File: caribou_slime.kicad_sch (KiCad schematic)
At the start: 38 parts, among them J1 BATT JST, Q1 AO3145, U1 ESP32-C3_SUPERMINI, U2 BMI270, U3 FS312F-G, U4 FS8205A, U5 TP4056, U6 ME6211C33M5G

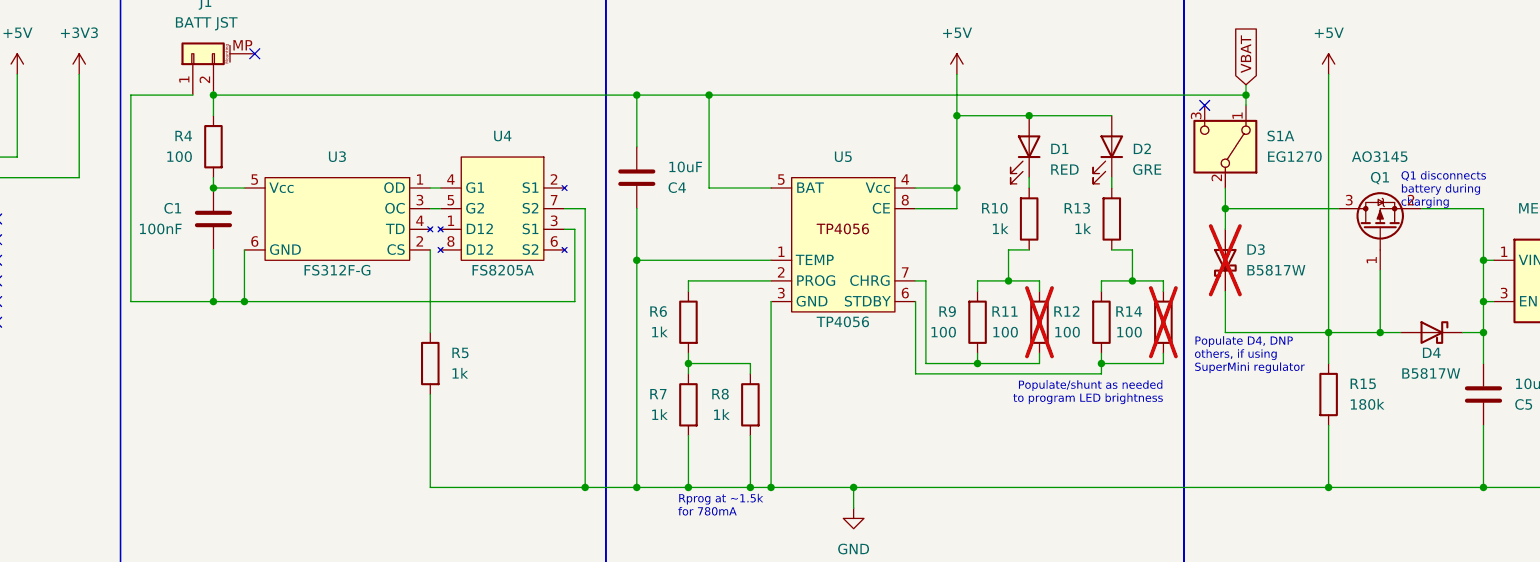
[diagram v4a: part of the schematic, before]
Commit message: fix(schematic): Make minor corrections to regulator circuit
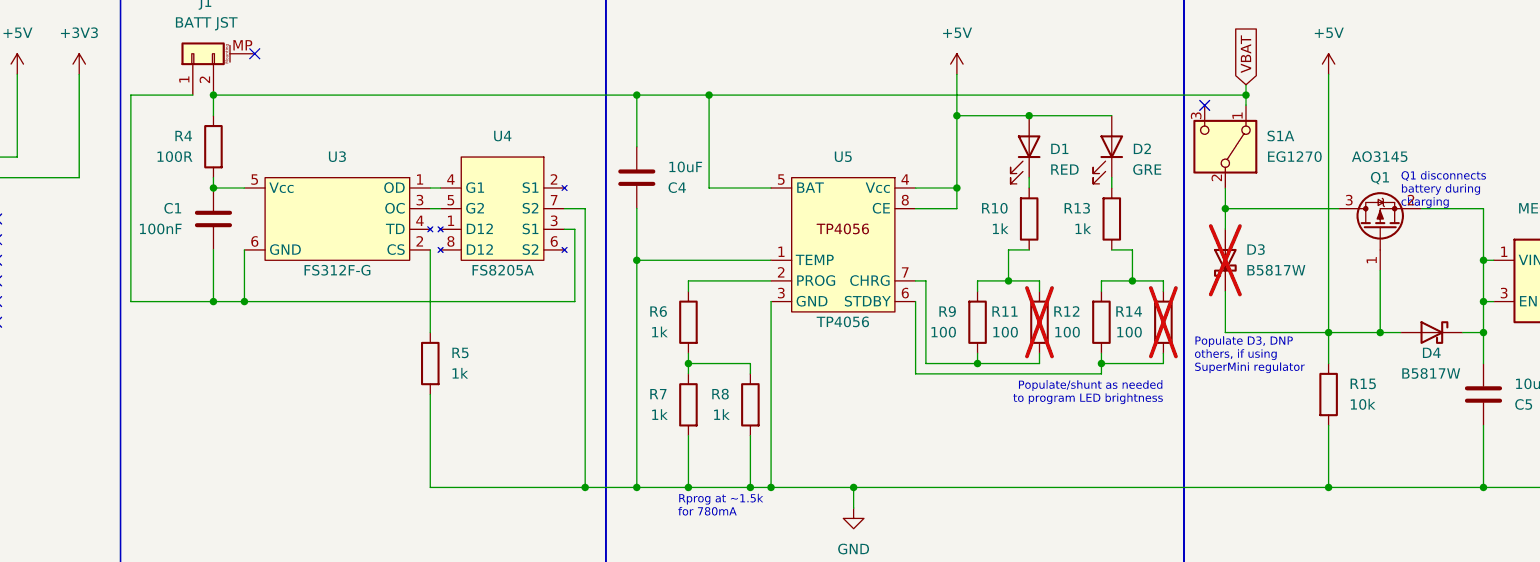
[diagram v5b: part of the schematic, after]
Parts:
- R15: value 180k -> 10k
- R4: value 100 -> 100R
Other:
- note added: "Populate D3, DNP others, if using SuperMini regulator"
- note removed: "Populate D4, DNP others, if using SuperMini regulator"
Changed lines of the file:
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@@
     (effects (font (size 1.27 1.27)) (justify left bottom))
   )
-  (text "Populate D4, DNP \nothers, if using\nSuperMini regulator"
+  (text "Populate D3, DNP \nothers, if using\nSuperMini regulator"
     (at 217.17 73.66 0)
     (effects (font (size 1 1)) (justify left bottom))
@@
       (effects (font (size 1.27 1.27)) (justify left))
     )
-    (property "Value" "100" (at 93.98 46.99 0)
+    (property "Value" "100R" (at 93.98 46.99 0)
       (effects (font (size 1.27 1.27)) (justify left))
     )
@@
       (effects (font (size 1.27 1.27)) (justify left))
     )
-    (property "Value" "180k" (at 236.22 77.47 0)
-      (effects (font (size 1.27 1.27)) (justify left))
-    )
+    (property "Value" "10k" (at 236.22 77.47 0)
+      (effects (font (size 1.27 1.27)) (justify left))
+    )

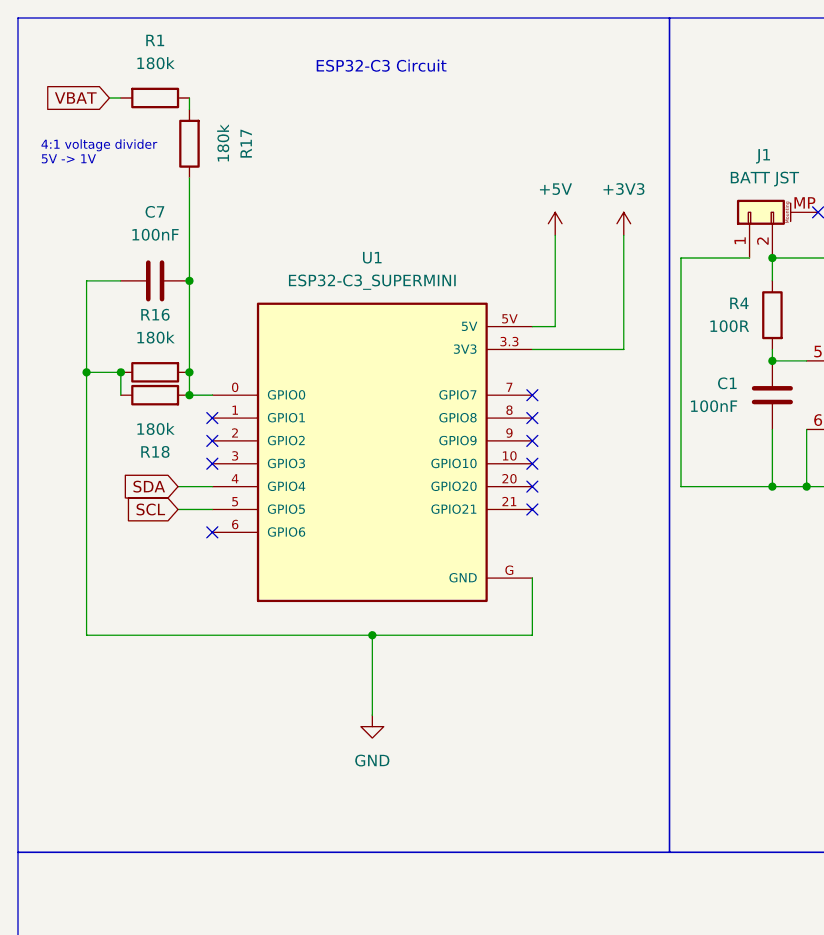
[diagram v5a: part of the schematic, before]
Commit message: fix(schematic): Correct battery sense voltage divider
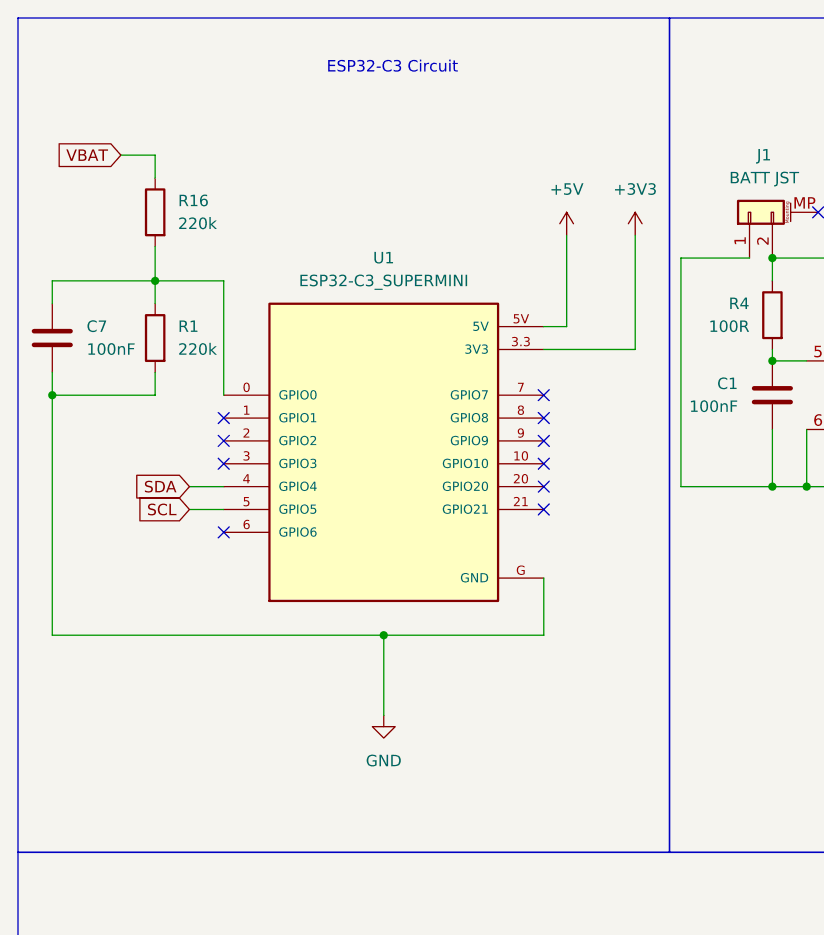
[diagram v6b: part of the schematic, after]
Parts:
- removed R17, R18: 180k, Resistor_SMD:R_0805_2012Metric, symbol Device:R
- R1, R16: value 180k -> 220k
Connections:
- net GND: now also R1.2; no longer R16.1
- net VBAT: now also R16.1; no longer R1.2
- net at R1.1: now also C7.2, R16.2, U1.0 (GPIO0)
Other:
- note removed: "4:1 voltage divider 5V -> 1V"
- moved on the sheet: C7, U1

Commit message: chore(pcb): Create and use BMI270 Hand Solder footprint
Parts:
- U2: footprint BMI270:XDCR_BMI270 -> BMI270:XDCR_BMI270_HandSolder
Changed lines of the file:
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@@
       (effects (font (size 1.27 1.27)))
     )
-    (property "Footprint" "BMI270:XDCR_BMI270" (at 92.71 161.29 0)
+    (property "Footprint" "BMI270:XDCR_BMI270_HandSolder" (at 92.71 161.29 0)
       (effects (font (size 1.27 1.27)) (justify bottom) hide)
     )

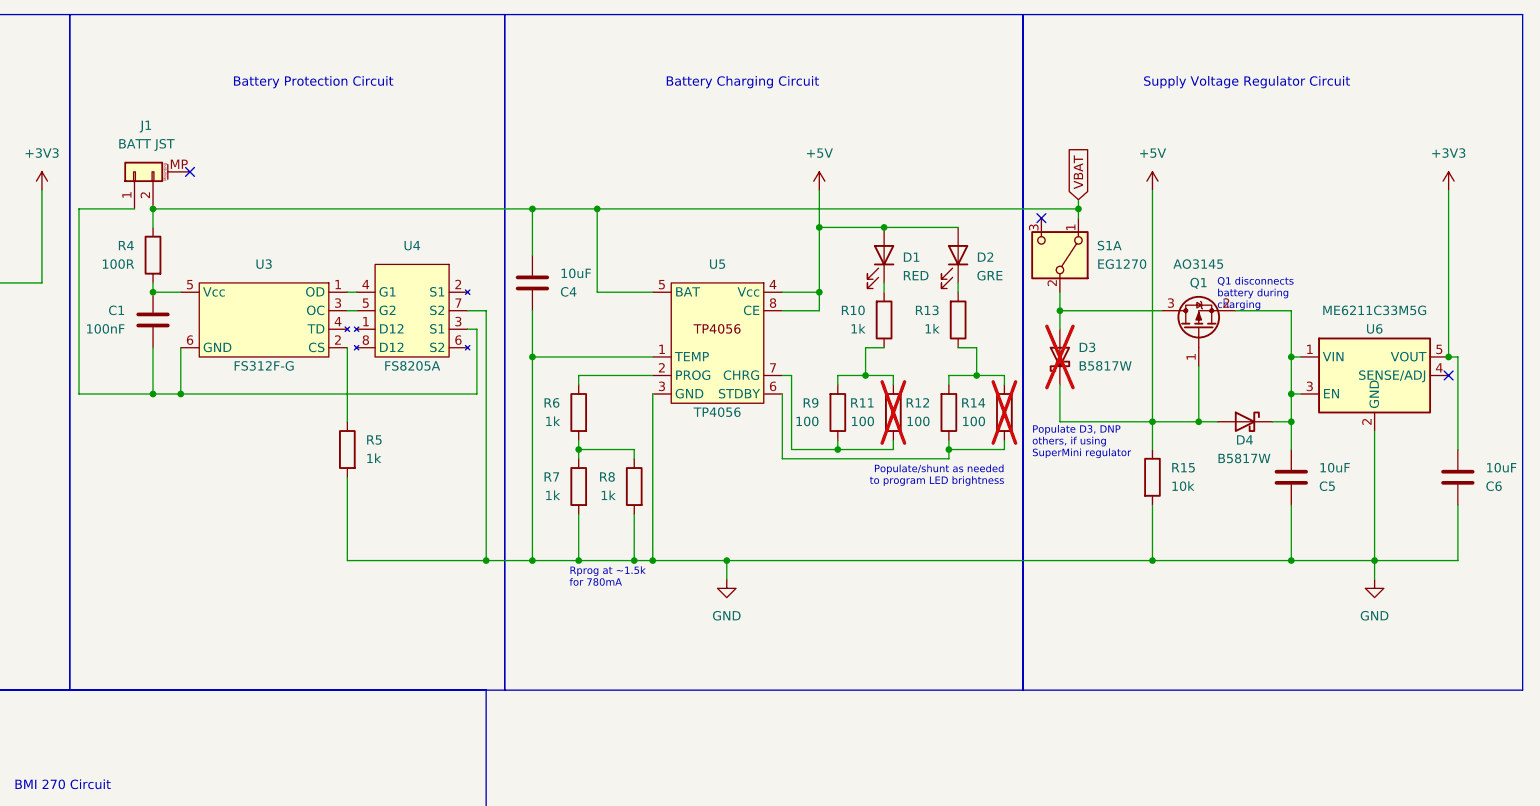
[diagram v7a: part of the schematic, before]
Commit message: fix(schematic): Move S1A to enable pin of regulator
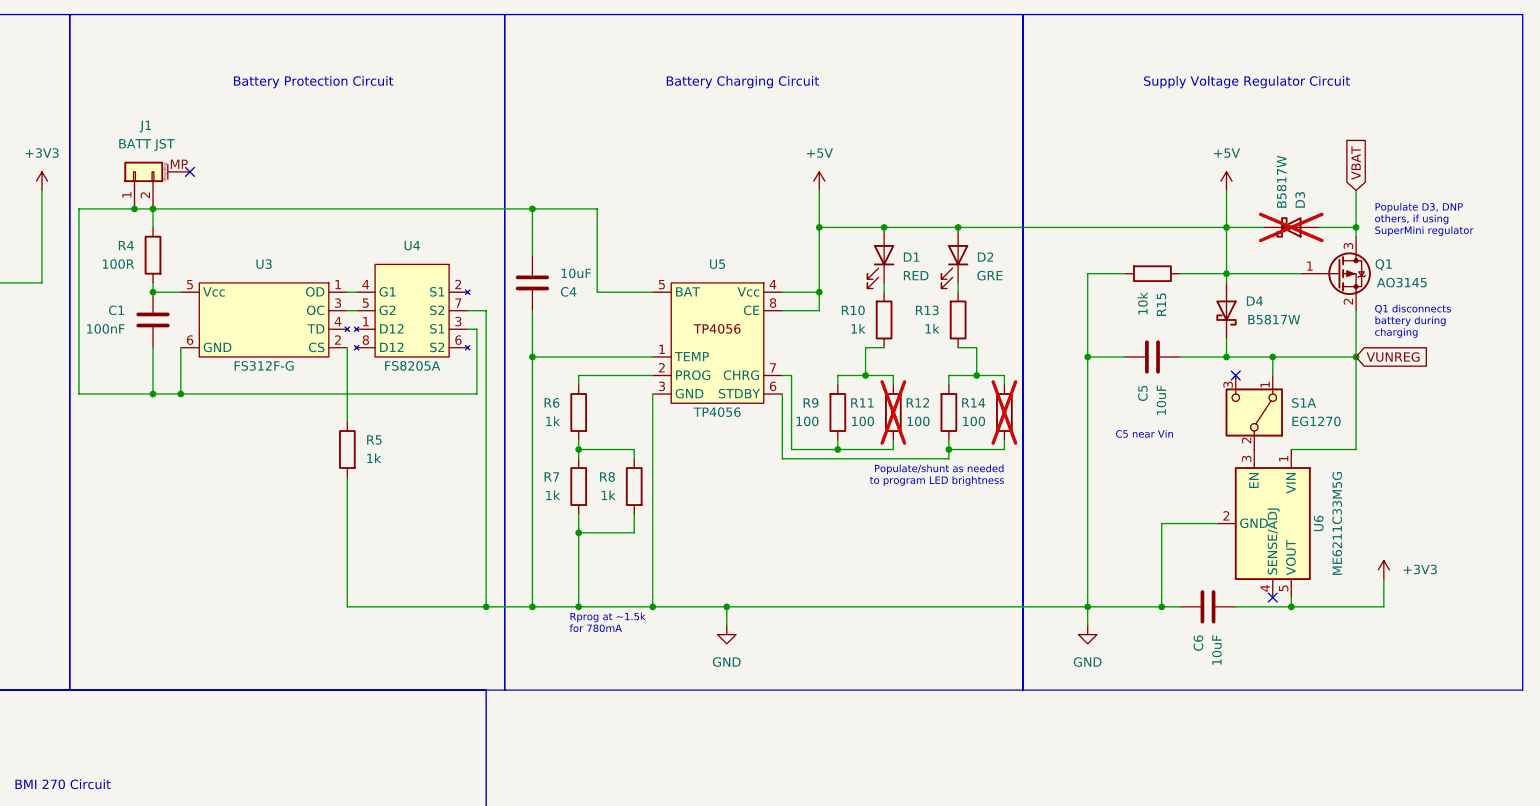
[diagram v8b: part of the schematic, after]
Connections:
- net VBAT: now also D3.2 (A), Q1.3 (D); no longer C4.2, J1.2 (Pin_2), R4.1, S1.1 (A), U5.5 (BAT)
- net VUNREG: now reaches C5.2, D4.1 (K), Q1.2 (S), U6.1 (VIN)
- net VUNREG: now also S1.1 (A); no longer U6.3 (EN)
- net at C1.2, J1.1 (Pin_1), U3.6 (GND)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: now also C4.2, J1.2 (Pin_2), R4.1, U5.5 (BAT)
- new net: S1.2 (B), U6.3 (EN)
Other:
- note added: "C5 near Vin"
- moved on the sheet: C5, C6, D3, D4, Q1, R15, S1A, U6
